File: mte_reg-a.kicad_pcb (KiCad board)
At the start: 2 copper layers, 95 x 75 mm, 82 parts, among them J1 GS2, J2 Conn_01x04, J3 GS2, J4 GS2, J5 Conn_02x04_Odd_Even, J6 MOLEX_KK-254, J7 MOLEX_KK-254, J8 Conn_01x10, J9 Conn_01x10, U1 LM317, U2 LM337, U3 LM317, U4 LM337

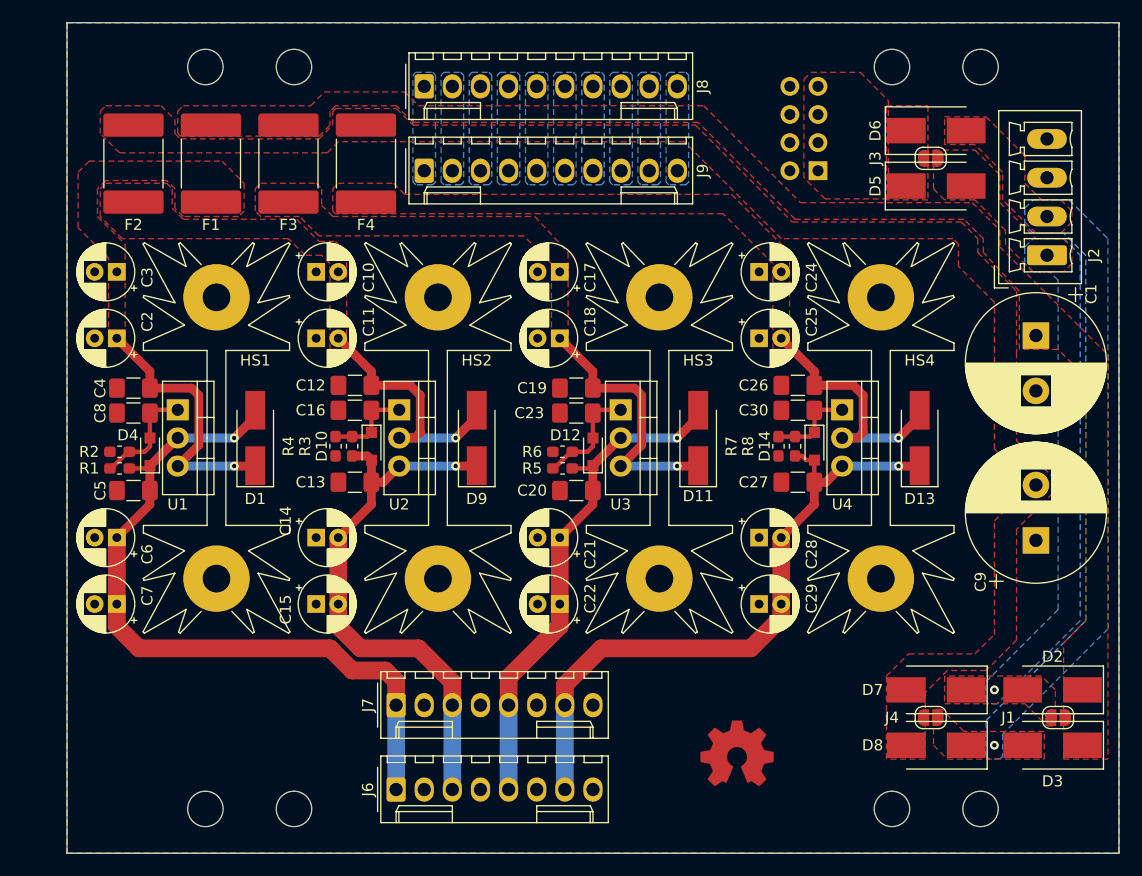
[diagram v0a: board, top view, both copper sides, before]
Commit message: Adjusted board width
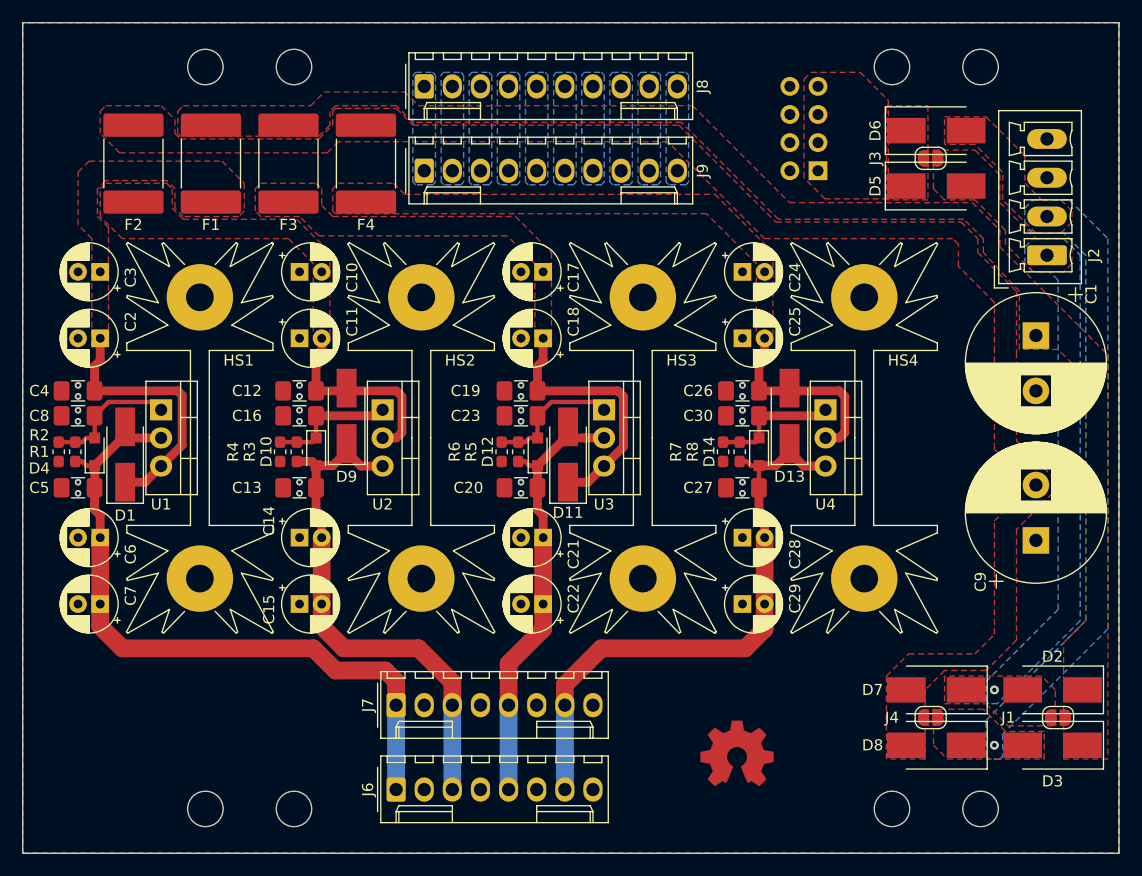
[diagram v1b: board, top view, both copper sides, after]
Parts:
- moved D13 11.9 mm to (197.8, 78.0)
- moved D9 11.9 mm to (157.8, 78.0)
- moved D1 11.8 mm to (137.8, 81.5)
- moved D11 11.8 mm to (177.8, 81.5)
- moved R2 5.50 mm to (131.8, 81.2), turned to 270 degrees
- moved R6 5.50 mm to (171.8, 81.2), turned to 270 degrees
- moved C12 5.02 mm to (153.5, 75.8)
- moved C13 5.02 mm to (153.5, 84.5)
- moved C16 5.02 mm to (153.5, 78.0)
- moved C26 5.02 mm to (193.5, 75.8)
- moved C27 5.02 mm to (193.5, 84.5)
- moved C30 5.02 mm to (193.5, 78.0)
- moved D10 5.02 mm to (155.0, 81.2)
- moved D14 5.02 mm to (195.0, 81.2)
- moved R3 5.02 mm to (153.2, 81.2)
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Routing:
- net Net-(C24-Pad2): track 24.2 -> 18.3 mm, vias 1 -> 0
- net Net-(C10-Pad2): track 24.1 -> 18.3 mm, vias 1 -> 0
- net /VCC2: track 46.4 -> 40.7 mm, vias 1 -> 0
- net /VEE2: track 59.0 -> 54.3 mm, vias 1 -> 0
- net Net-(C30-Pad1): track 7.94 -> 11.6 mm
- net Net-(C16-Pad1): track 7.94 -> 11.6 mm
- net /VCC1: track 67.5 -> 63.9 mm, vias 1 -> 0
- net Net-(C8-Pad1): track 10.1 -> 12.6 mm
- net Net-(C23-Pad1): track 10.1 -> 12.2 mm
- net /VEE1: track 50.4 -> 48.8 mm, vias 1 -> 0
- net Net-(C17-Pad1): track 24.6 -> 23.8 mm, vias 1 -> 0
- net Net-(C2-Pad1): track 24.6 -> 24.1 mm, vias 1 -> 0
- net AGND: vias 0 -> 24
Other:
- board size 95 x 75 mm -> 99 x 75 mm
